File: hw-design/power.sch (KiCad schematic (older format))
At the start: 14 parts, among them CN1 CONN_02X02, CN2 CONN_02X02, U1 AP1117E50, U2 AP1117E33

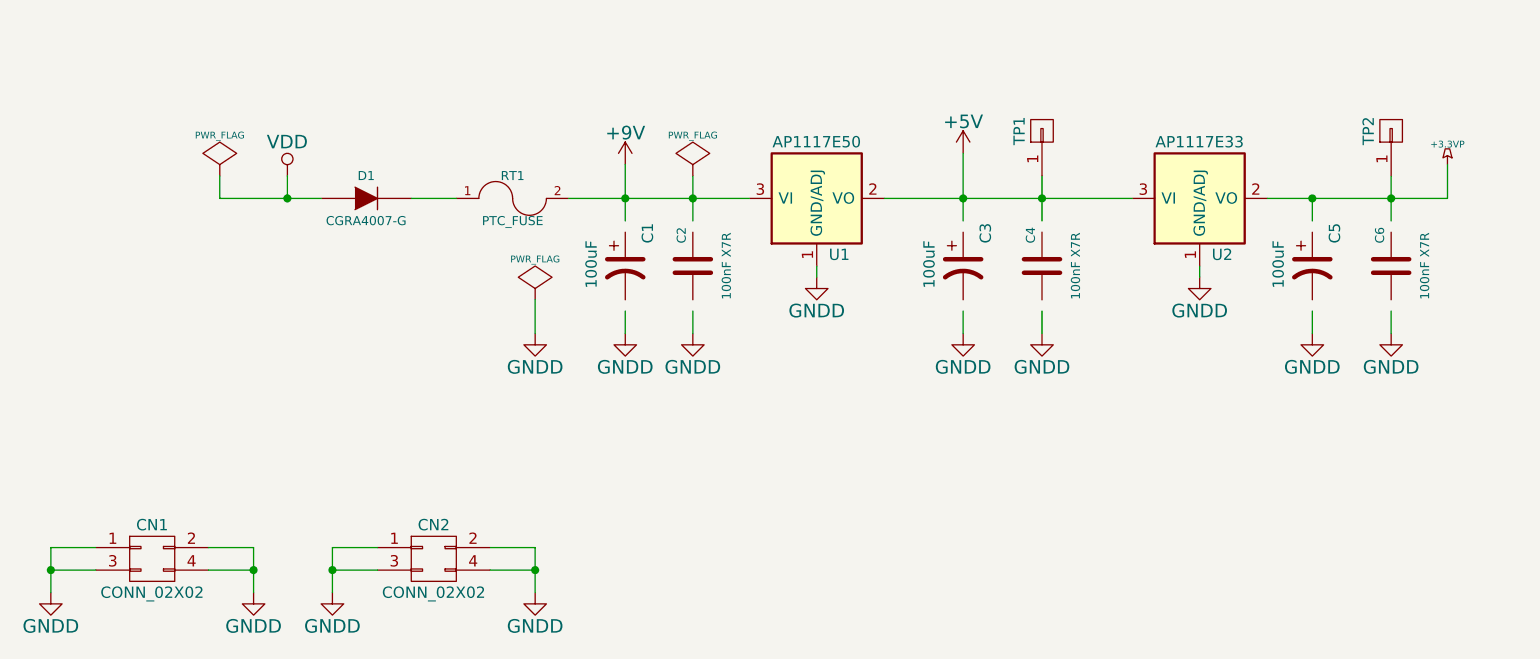
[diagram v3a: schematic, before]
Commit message: adding official kicad library as submodule
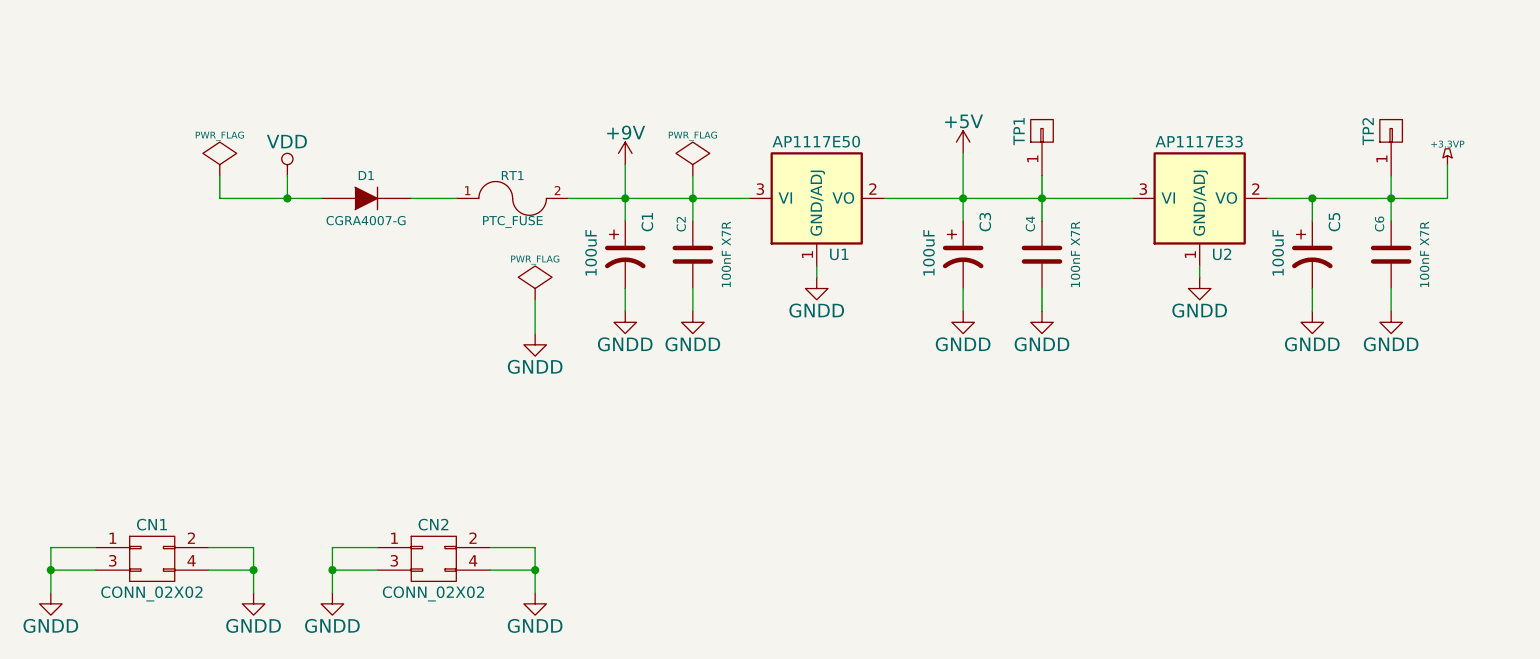
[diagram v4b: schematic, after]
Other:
- moved on the sheet: C1, C2, C3, C4, C5, C6
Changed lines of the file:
@@
 L CP1 C5
 U 1 1 548B65E4
-P 7100 2300
-F 0 "C5" V 7200 2400 50  0000 L CNN
-F 1 "100uF" V 6950 2200 50  0000 L CNN
-F 2 "Capacitors_ThroughHole:Capacitor5x6RM2.5" H 7100 2300 60  0001 C CNN
-F 3 "~" H 7100 2300 60  0000 C CNN
-	1    7100 2300
+P 7100 2250
+F 0 "C5" V 7200 2350 50  0000 L CNN
+F 1 "100uF" V 6950 2150 50  0000 L CNN
+F 2 "Capacitors_ThroughHole:Capacitor5x6RM2.5" H 7100 2250 60  0001 C CNN
+F 3 "~" H 7100 2250 60  0000 C CNN
+	1    7100 2250
 	1    0    0    -1
 $EndComp
@@
 L CP1 C3
 U 1 1 548B65F7
-P 5550 2300
-F 0 "C3" V 5650 2400 50  0000 L CNN
-F 1 "100uF" V 5400 2200 50  0000 L CNN
-F 2 "Capacitors_ThroughHole:Capacitor5x6RM2.5" H 5550 2300 60  0001 C CNN
-F 3 "~" H 5550 2300 60  0000 C CNN
-	1    5550 2300
+P 5550 2250
+F 0 "C3" V 5650 2350 50  0000 L CNN
+F 1 "100uF" V 5400 2150 50  0000 L CNN
+F 2 "Capacitors_ThroughHole:Capacitor5x6RM2.5" H 5550 2250 60  0001 C CNN
+F 3 "~" H 5550 2250 60  0000 C CNN
+	1    5550 2250
 	1    0    0    -1
 $EndComp
@@
 L C C6
 U 1 1 548B660A
-P 7450 2300
-F 0 "C6" V 7400 2400 40  0000 L CNN
-F 1 "100nF X7R" V 7600 2150 40  0000 L CNN
-F 2 "Capacitors_SMD:C_0603" H 7488 2150 30  0001 C CNN
-F 3 "~" H 7450 2300 60  0000 C CNN
-	1    7450 2300
+P 7450 2250
+F 0 "C6" V 7400 2350 40  0000 L CNN
+F 1 "100nF X7R" V 7600 2100 40  0000 L CNN
+F 2 "Capacitors_SMD:C_0603" H 7488 2100 30  0001 C CNN
+F 3 "~" H 7450 2250 60  0000 C CNN
+	1    7450 2250
 	1    0    0    -1
 $EndComp
@@
 L C C4
 U 1 1 548B6624
-P 5900 2300
-F 0 "C4" V 5850 2400 40  0000 L CNN
-F 1 "100nF X7R" V 6050 2150 40  0000 L CNN
-F 2 "Capacitors_SMD:C_0603" H 5938 2150 30  0001 C CNN
-F 3 "~" H 5900 2300 60  0000 C CNN
-	1    5900 2300
+P 5900 2250
+F 0 "C4" V 5850 2350 40  0000 L CNN
+F 1 "100nF X7R" V 6050 2100 40  0000 L CNN
+F 2 "Capacitors_SMD:C_0603" H 5938 2100 30  0001 C CNN
+F 3 "~" H 5900 2250 60  0000 C CNN
+	1    5900 2250
 	1    0    0    -1
 $EndComp
@@
 L CP1 C1
 U 1 1 548B663E
-P 4050 2300
-F 0 "C1" V 4150 2400 50  0000 L CNN
-F 1 "100uF" V 3900 2200 50  0000 L CNN
-F 2 "Capacitors_ThroughHole:Capacitor5x6RM2.5" H 4050 2300 60  0001 C CNN
-F 3 "~" H 4050 2300 60  0000 C CNN
-	1    4050 2300
+P 4050 2250
+F 0 "C1" V 4150 2350 50  0000 L CNN
+F 1 "100uF" V 3900 2150 50  0000 L CNN
+F 2 "Capacitors_ThroughHole:Capacitor5x6RM2.5" H 4050 2250 60  0001 C CNN
+F 3 "~" H 4050 2250 60  0000 C CNN
+	1    4050 2250
 	1    0    0    -1
 $EndComp
@@
 L C C2
 U 1 1 548B665F
-P 4350 2300
-F 0 "C2" V 4300 2400 40  0000 L CNN
-F 1 "100nF X7R" V 4500 2150 40  0000 L CNN
-F 2 "Capacitors_SMD:C_0603" H 4388 2150 30  0001 C CNN
-F 3 "~" H 4350 2300 60  0000 C CNN
-	1    4350 2300
+P 4350 2250
+F 0 "C2" V 4300 2350 40  0000 L CNN
+F 1 "100nF X7R" V 4500 2100 40  0000 L CNN
+F 2 "Capacitors_SMD:C_0603" H 4388 2100 30  0001 C CNN
+F 3 "~" H 4350 2250 60  0000 C CNN
+	1    4350 2250
 	1    0    0    -1
 $EndComp
@@
 $EndComp
 Wire Wire Line
-	5550 2500 5550 2600
-Wire Wire Line
-	7100 2600 7100 2500
+	5550 2400 5550 2500
+Wire Wire Line
+	7100 2500 7100 2400
 Wire Wire Line
 	7100 2000 7100 2100
@@
 Connection ~ 5550 2000
 Wire Wire Line
-	7450 2600 7450 2500
+	7450 2500 7450 2400
 Connection ~ 7450 2000
 Wire Wire Line
 	7700 2000 7700 1850
 Wire Wire Line
-	5900 2500 5900 2600
-Wire Wire Line
-	4050 2500 4050 2600
+	5900 2400 5900 2500
+Wire Wire Line
+	4050 2400 4050 2500
 Wire Wire Line
 	4050 1850 4050 2100
 Connection ~ 4050 2000
 Wire Wire Line
-	4350 2500 4350 2600
+	4350 2400 4350 2500
 Wire Wire Line
 	4350 1900 4350 2100
@@
 L GNDD #PWR06
 U 1 1 54E7EE6C
-P 4050 2600
-F 0 "#PWR06" H 4050 2350 60  0001 C CNN
-F 1 "GNDD" H 4050 2450 60  0000 C CNN
-F 2 "" H 4050 2600 60  0000 C CNN
-F 3 "" H 4050 2600 60  0000 C CNN
-	1    4050 2600
+P 4050 2500
+F 0 "#PWR06" H 4050 2250 60  0001 C CNN
+F 1 "GNDD" H 4050 2350 60  0000 C CNN
+F 2 "" H 4050 2500 60  0000 C CNN
+F 3 "" H 4050 2500 60  0000 C CNN
+	1    4050 2500
 	1    0    0    -1
 $EndComp
@@
 L GNDD #PWR07
 U 1 1 54E7EE80
-P 4350 2600
-F 0 "#PWR07" H 4350 2350 60  0001 C CNN
-F 1 "GNDD" H 4350 2450 60  0000 C CNN
-F 2 "" H 4350 2600 60  0000 C CNN
-F 3 "" H 4350 2600 60  0000 C CNN
-	1    4350 2600
+P 4350 2500
+F 0 "#PWR07" H 4350 2250 60  0001 C CNN
+F 1 "GNDD" H 4350 2350 60  0000 C CNN
+F 2 "" H 4350 2500 60  0000 C CNN
+F 3 "" H 4350 2500 60  0000 C CNN
+	1    4350 2500
 	1    0    0    -1
 $EndComp
@@
 L GNDD #PWR012
 U 1 1 54E7F9F2
-P 5550 2600
-F 0 "#PWR012" H 5550 2350 60  0001 C CNN
-F 1 "GNDD" H 5550 2450 60  0000 C CNN
-F 2 "" H 5550 2600 60  0000 C CNN
-F 3 "" H 5550 2600 60  0000 C CNN
-	1    5550 2600
+P 5550 2500
+F 0 "#PWR012" H 5550 2250 60  0001 C CNN
+F 1 "GNDD" H 5550 2350 60  0000 C CNN
+F 2 "" H 5550 2500 60  0000 C CNN
+F 3 "" H 5550 2500 60  0000 C CNN
+	1    5550 2500
 	1    0    0    -1
 $EndComp
@@
 L GNDD #PWR013
 U 1 1 54E7FA28
-P 5900 2600
-F 0 "#PWR013" H 5900 2350 60  0001 C CNN
-F 1 "GNDD" H 5900 2450 60  0000 C CNN
-F 2 "" H 5900 2600 60  0000 C CNN
-F 3 "" H 5900 2600 60  0000 C CNN
-	1    5900 2600
+P 5900 2500
+F 0 "#PWR013" H 5900 2250 60  0001 C CNN
+F 1 "GNDD" H 5900 2350 60  0000 C CNN
+F 2 "" H 5900 2500 60  0000 C CNN
+F 3 "" H 5900 2500 60  0000 C CNN
+	1    5900 2500
 	1    0    0    -1
 $EndComp
@@
 L GNDD #PWR014
 U 1 1 54E7FA3C
-P 7100 2600
-F 0 "#PWR014" H 7100 2350 60  0001 C CNN
-F 1 "GNDD" H 7100 2450 60  0000 C CNN
-F 2 "" H 7100 2600 60  0000 C CNN
-F 3 "" H 7100 2600 60  0000 C CNN
-	1    7100 2600
+P 7100 2500
+F 0 "#PWR014" H 7100 2250 60  0001 C CNN
+F 1 "GNDD" H 7100 2350 60  0000 C CNN
+F 2 "" H 7100 2500 60  0000 C CNN
+F 3 "" H 7100 2500 60  0000 C CNN
+	1    7100 2500
 	1    0    0    -1
 $EndComp
@@
 L GNDD #PWR015
 U 1 1 54E7FA50
-P 7450 2600
-F 0 "#PWR015" H 7450 2350 60  0001 C CNN
-F 1 "GNDD" H 7450 2450 60  0000 C CNN
-F 2 "" H 7450 2600 60  0000 C CNN
-F 3 "" H 7450 2600 60  0000 C CNN
-	1    7450 2600
-	1    0    0    -1
-$EndComp
+P 7450 2500
+F 0 "#PWR015" H 7450 2250 60  0001 C CNN
+F 1 "GNDD" H 7450 2350 60  0000 C CNN
+F 2 "" H 7450 2500 60  0000 C CNN
+F 3 "" H 7450 2500 60  0000 C CNN
+	1    7450 2500
+	1    0    0    -1
+$EndComp

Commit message: replacing some cached symbols by kicad-library symbols
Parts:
- D1: symbol DIODE -> D
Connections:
- net VDD: now also D1.2 (A); no longer D1.1 (A)
- net at RT1.1: now also D1.1 (K); no longer D1.2 (K)
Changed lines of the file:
@@
 $EndComp
 $Comp
-L DIODE D1
+L D D1
 U 1 1 548B6651
 P 2900 2000
@@
 F 3 "~" H 2900 2000 60  0000 C CNN
 	1    2900 2000
-	1    0    0    -1
+	-1   0    0    1
 $EndComp
 $Comp
@@
 Connection ~ 4350 2000
 Wire Wire Line
-	3100 2000 3300 2000
+	3050 2000 3300 2000
 Wire Wire Line
 	5900 1900 5900 2100
@@
 	5550 1800 5550 2100
 Wire Wire Line
-	2250 2000 2700 2000
+	2250 2000 2750 2000
 Wire Wire Line
 	3650 2450 3650 2600

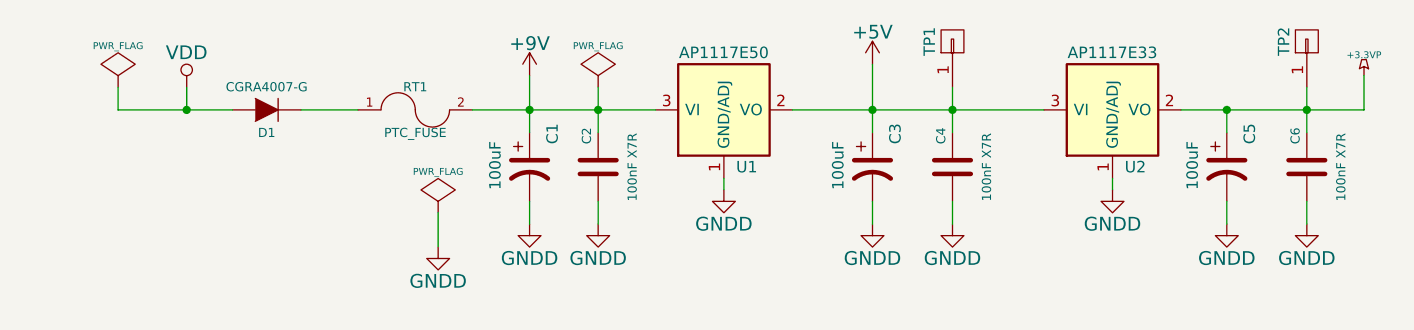
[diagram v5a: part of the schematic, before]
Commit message: sch: updating some cached symbols
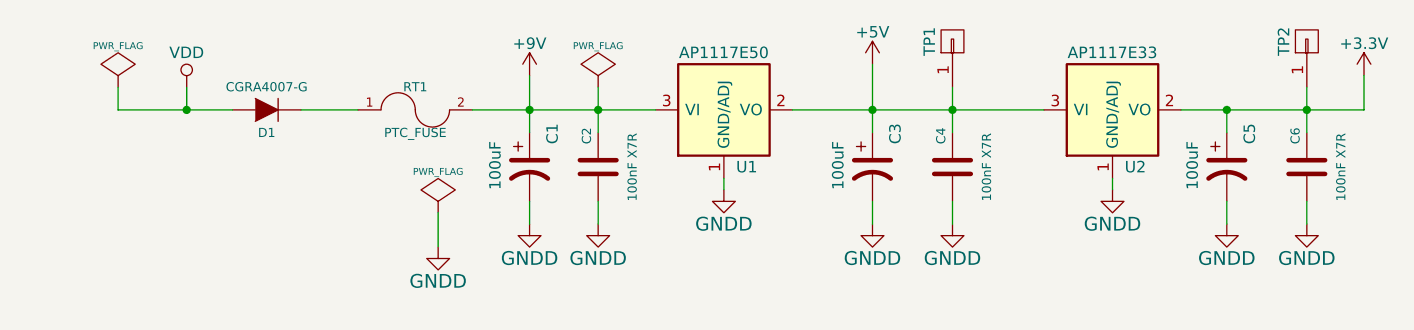
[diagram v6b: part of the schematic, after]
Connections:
- net +3.3VP renamed +3V3
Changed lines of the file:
@@
 LIBS:conn
 LIBS:interface
-LIBS:expression-pedal-cache
 EELAYER 25 0
 EELAYER END
@@
 U 1 1 54E7D8DE
 P 2550 1900
-F 0 "#PWR04" H 2550 1750 60  0001 C CNN
-F 1 "VDD" H 2550 2050 60  0000 C CNN
+F 0 "#PWR04" H 2550 1750 50  0001 C CNN
+F 1 "VDD" H 2550 2050 50  0000 C CNN
 F 2 "" H 2550 1900 60  0000 C CNN
 F 3 "" H 2550 1900 60  0000 C CNN
@@
 U 1 1 54E80C28
 P 5550 1800
-F 0 "#PWR017" H 5550 1650 60  0001 C CNN
-F 1 "+5V" H 5550 1940 60  0000 C CNN
+F 0 "#PWR017" H 5550 1650 50  0001 C CNN
+F 1 "+5V" H 5550 1940 50  0000 C CNN
 F 2 "" H 5550 1800 60  0000 C CNN
 F 3 "" H 5550 1800 60  0000 C CNN
 	1    5550 1800
-	1    0    0    -1
-$EndComp
-$Comp
-L +3.3VP #PWR018
-U 1 1 54E84DA1
-P 7700 1850
-F 0 "#PWR018" H 7750 1880 20  0001 C CNN
-F 1 "+3.3VP" H 7700 1940 30  0000 C CNN
-F 2 "" H 7700 1850 60  0000 C CNN
-F 3 "" H 7700 1850 60  0000 C CNN
-	1    7700 1850
 	1    0    0    -1
 $EndComp
@@
 Wire Wire Line
 	6600 2300 6600 2350
-$Comp
-L +9V #PWR020
-U 1 1 54E893A4
-P 4050 1850
-F 0 "#PWR020" H 4050 1700 60  0001 C CNN
-F 1 "+9V" H 4050 1990 60  0000 C CNN
-F 2 "" H 4050 1850 60  0000 C CNN
-F 3 "" H 4050 1850 60  0000 C CNN
-	1    4050 1850
-	1    0    0    -1
-$EndComp
 $Comp
 L CONN_02X02 CN1
@@
 Wire Wire Line
 	6900 2000 7700 2000
+$Comp
+L +3.3V #PWR?
+U 1 1 556EF2E1
+P 7700 1850
+F 0 "#PWR?" H 7700 1700 50  0001 C CNN
+F 1 "+3.3V" H 7700 1990 50  0000 C CNN
+F 2 "" H 7700 1850 60  0000 C CNN
+F 3 "" H 7700 1850 60  0000 C CNN
+	1    7700 1850
+	1    0    0    -1
+$EndComp
+$Comp
+L +9V #PWR?
+U 1 1 556F8AA1
+P 4050 1850
+F 0 "#PWR?" H 4050 1700 50  0001 C CNN
+F 1 "+9V" H 4050 1990 50  0000 C CNN
+F 2 "" H 4050 1850 60  0000 C CNN
+F 3 "" H 4050 1850 60  0000 C CNN
+	1    4050 1850
+	1    0    0    -1
+$EndComp
 $EndSCHEMATC
